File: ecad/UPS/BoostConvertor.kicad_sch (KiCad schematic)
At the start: 24 parts

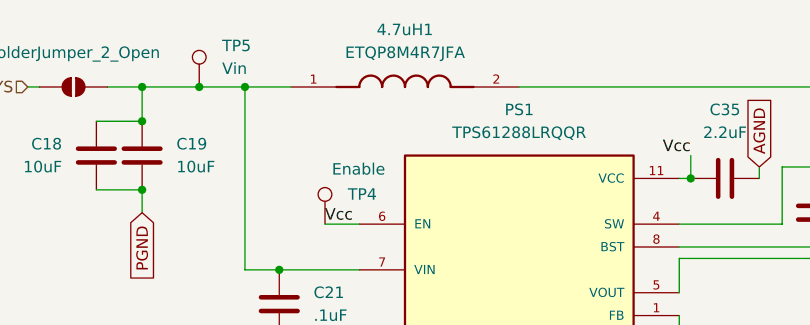
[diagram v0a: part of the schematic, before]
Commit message: Add switch
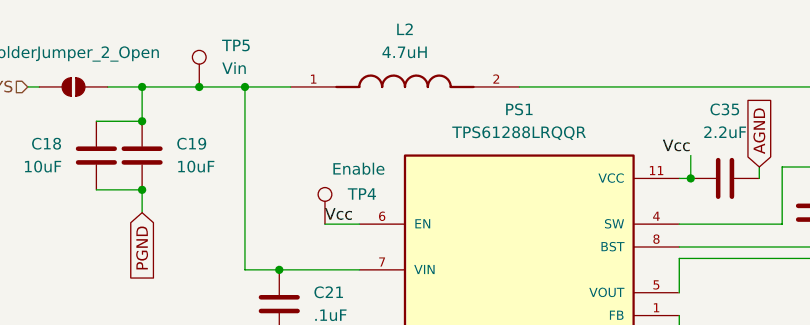
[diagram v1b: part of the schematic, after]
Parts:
- L2: renamed from 4.7uH1; value ETQP8M4R7JFA -> 4.7uH; footprint ETQP8M4R7JFA:IND_ETQP8M4R7JFA -> UPS:IND_ETQP8M4R7JFA
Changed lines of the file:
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@@
 		(dnp no)
 		(fields_autoplaced yes)
-		(property "Reference" "4.7uH1"
+		(property "Reference" "L2"
 			(at 92.71 45.72 0)
 			(effects
@@
 			)
 		)
-		(property "Value" "ETQP8M4R7JFA"
+		(property "Value" "4.7uH"
 			(at 92.71 48.26 0)
 			(effects
@@
 			)
 		)
-		(property "Footprint" "ETQP8M4R7JFA:IND_ETQP8M4R7JFA"
+		(property "Footprint" "UPS:IND_ETQP8M4R7JFA"
 			(at 92.71 52.07 0)
 			(effects
@@
 			(project ""
 				(path "/9d92b60a-4a6b-449c-b462-cab19e69d38c/66173f08-558e-4192-bd35-ba55c00529e3"
-					(reference "4.7uH1")
+					(reference "L2")
 					(unit 1)
 				)

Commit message: Output section of PCB
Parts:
- PS1: footprint TPS61288LRQQR:CONV_TPS61288LRQQR -> UPS:CONV_TPS61288LRQQR
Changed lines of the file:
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@@
 			)
 		)
-		(property "Footprint" "TPS61288LRQQR:CONV_TPS61288LRQQR"
+		(property "Footprint" "UPS:CONV_TPS61288LRQQR"
 			(at 105.41 77.47 0)
 			(effects

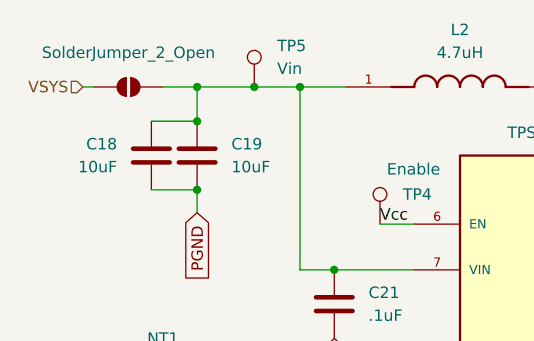
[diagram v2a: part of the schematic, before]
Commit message: replaced solder jumper with resistor
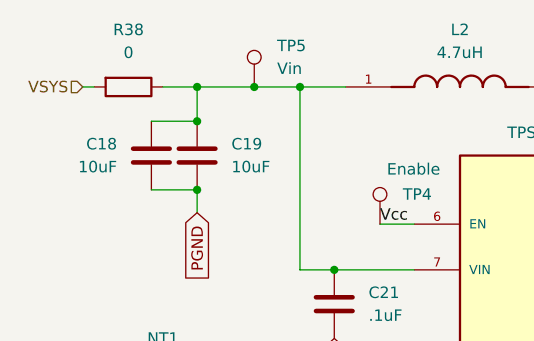
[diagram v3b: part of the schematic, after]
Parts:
- removed JP1: SolderJumper_2_Open, Jumper:SolderJumper-2_P1.3mm_Open_Pad1.0x1.5mm, symbol Jumper:SolderJumper_2_Open
- added R38: 0, Resistor_SMD:R_0805_2012Metric, symbol Device:R
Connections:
- net VSYS: now also R38.2
- net at C18.1, C19.1, C21.1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: now also R38.1
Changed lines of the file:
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@@
+	)
+	(symbol
+		(lib_id "Device:R")
+		(at 55.88 52.07 270)
+		(unit 1)
+		(exclude_from_sim no)
+		(in_bom yes)
+		(on_board yes)
+		(dnp no)
+		(fields_autoplaced yes)
+		(property "Reference" "R38"
+			(at 55.88 45.72 90)
+			(effects
+				(font
+					(size 1.27 1.27)
+				)
+			)
+		)
+		(property "Value" "0"
+			(at 55.88 48.26 90)
+			(effects
+				(font
+					(size 1.27 1.27)
+				)
+			)
+		)
+		(property "Footprint" "Resistor_SMD:R_0805_2012Metric"
+			(at 55.88 50.292 90)
+			(effects
+				(font
+					(size 1.27 1.27)
+				)
+				(hide yes)
+			)
+		)
+		(property "Datasheet" "~"
+			(at 55.88 52.07 0)
+			(effects
+				(font
+					(size 1.27 1.27)
+				)
+				(hide yes)
+			)
+		)
+		(property "Description" "Resistor"
+			(at 55.88 52.07 0)
+			(effects
+				(font
+					(size 1.27 1.27)
+				)
+				(hide yes)
+			)
+		)
+		(pin "2"
+		)
+		(pin "1"
+		)
+		(instances
+			(project ""
+				(path "/9d92b60a-4a6b-449c-b462-cab19e69d38c/66173f08-558e-4192-bd35-ba55c00529e3"
+					(reference "R38")
+					(unit 1)
+				)
+			)
+		)
 	)
 	(symbol
@@
 					(unit 1)
 				)
-			)
-		)
-	)
-	(symbol
-		(lib_id "Jumper:SolderJumper_2_Open")
-		(at 55.88 52.07 0)
-		(unit 1)
-		(exclude_from_sim no)
-		(in_bom no)
-		(on_board yes)
-		(dnp no)
-		(fields_autoplaced yes)
-		(property "Reference" "JP1"
-			(at 55.88 45.72 0)
-			(effects
-				(font
-					(size 1.27 1.27)
-				)
-				(hide yes)
-			)
-		)
-		(property "Value" "SolderJumper_2_Open"
-			(at 55.88 48.26 0)
-			(effects
-				(font
-					(size 1.27 1.27)
-				)
-			)
-		)
-		(property "Footprint" "Jumper:SolderJumper-2_P1.3mm_Open_Pad1.0x1.5mm"
-			(at 55.88 52.07 0)
-			(effects
-				(font
-					(size 1.27 1.27)
-				)
-				(hide yes)
-			)
-		)
-		(property "Datasheet" "~"
-			(at 55.88 52.07 0)
-			(effects
-				(font
-					(size 1.27 1.27)
-				)
-				(hide yes)
-			)
-		)
-		(property "Description" "Solder Jumper, 2-pole, open"
-			(at 55.88 52.07 0)
-			(effects
-				(font
-					(size 1.27 1.27)
-				)
-				(hide yes)
-			)
-		)
-		(pin "1"
-		)
-		(pin "2"
-		)
-		(instances
-			(project ""
-				(path "/9d92b60a-4a6b-449c-b462-cab19e69d38c/66173f08-558e-4192-bd35-ba55c00529e3"
-					(reference "JP1")
-					(unit 1)
-				)

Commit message: Updated Footprints
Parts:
- C20, C21, C22, C23, C3, C36: footprint Capacitor_SMD:C_0402_1005Metric_Pad0.74x0.62mm_HandSolder -> Capacitor_SMD:C_0603_1608Metric_Pad1.08x0.95mm_HandSolder
- R30, R31, R32: footprint Capacitor_SMD:C_0603_1608Metric_Pad1.08x0.95mm_HandSolder -> Resistor_SMD:R_0603_1608Metric_Pad0.98x0.95mm_HandSolder
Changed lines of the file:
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@@
 			)
 		)
-		(property "Footprint" "Capacitor_SMD:C_0402_1005Metric_Pad0.74x0.62mm_HandSolder"
+		(property "Footprint" "Capacitor_SMD:C_0603_1608Metric_Pad1.08x0.95mm_HandSolder"
 			(at 139.3952 69.85 0)
 			(effects
@@
 			)
 		)
-		(property "Footprint" "Capacitor_SMD:C_0402_1005Metric_Pad0.74x0.62mm_HandSolder"
+		(property "Footprint" "Capacitor_SMD:C_0603_1608Metric_Pad1.08x0.95mm_HandSolder"
 			(at 168.6052 87.63 0)
 			(effects
@@
 			)
 		)
-		(property "Footprint" "Capacitor_SMD:C_0603_1608Metric_Pad1.08x0.95mm_HandSolder"
+		(property "Footprint" "Resistor_SMD:R_0603_1608Metric_Pad0.98x0.95mm_HandSolder"
 			(at 135.382 93.98 90)
 			(effects
@@
 			)
 		)
-		(property "Footprint" "Capacitor_SMD:C_0402_1005Metric_Pad0.74x0.62mm_HandSolder"
+		(property "Footprint" "Capacitor_SMD:C_0603_1608Metric_Pad1.08x0.95mm_HandSolder"
 			(at 147.0152 90.17 0)
 			(effects
@@
 			)
 		)
-		(property "Footprint" "Capacitor_SMD:C_0402_1005Metric_Pad0.74x0.62mm_HandSolder"
+		(property "Footprint" "Capacitor_SMD:C_0603_1608Metric_Pad1.08x0.95mm_HandSolder"
 			(at 79.7052 80.01 0)
 			(effects
@@
 			)
 		)
-		(property "Footprint" "Capacitor_SMD:C_0603_1608Metric_Pad1.08x0.95mm_HandSolder"
+		(property "Footprint" "Resistor_SMD:R_0603_1608Metric_Pad0.98x0.95mm_HandSolder"
 			(at 155.702 74.93 90)
 			(effects
@@
 			)
 		)
-		(property "Footprint" "Capacitor_SMD:C_0402_1005Metric_Pad0.74x0.62mm_HandSolder"
+		(property "Footprint" "Capacitor_SMD:C_0603_1608Metric_Pad1.08x0.95mm_HandSolder"
 			(at 136.1948 82.55 0)
 			(effects
@@
 			)
 		)
-		(property "Footprint" "Capacitor_SMD:C_0603_1608Metric_Pad1.08x0.95mm_HandSolder"
+		(property "Footprint" "Resistor_SMD:R_0603_1608Metric_Pad0.98x0.95mm_HandSolder"
 			(at 155.702 85.09 90)
 			(effects
@@
 			)
 		)
-		(property "Footprint" "Capacitor_SMD:C_0402_1005Metric_Pad0.74x0.62mm_HandSolder"
+		(property "Footprint" "Capacitor_SMD:C_0603_1608Metric_Pad1.08x0.95mm_HandSolder"
 			(at 172.4152 78.74 0)
 			(effects

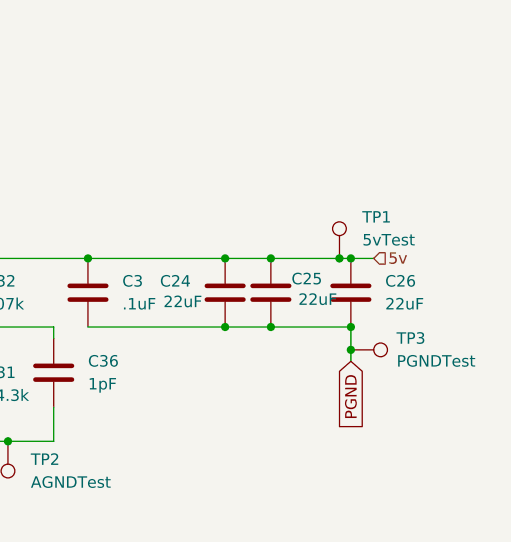
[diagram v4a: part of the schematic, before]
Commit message: Ty's VBATSENSE Changes
Let me know if I messed this part up, did a small amount
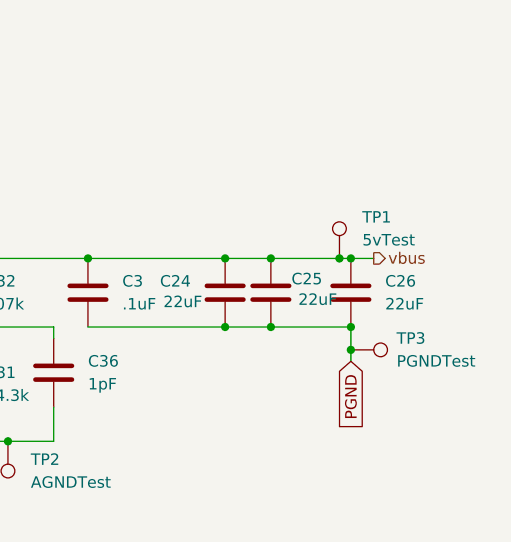
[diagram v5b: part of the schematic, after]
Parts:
- NT1: footprint (none) -> NetTie:NetTie-4_THT_Pad1.0mm
- R38: footprint Resistor_SMD:R_0805_2012Metric -> Resistor_SMD:R_1218_3246Metric_Pad1.22x4.75mm_HandSolder
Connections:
- net 5v renamed vbus
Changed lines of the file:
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@@
 		)
 	)
-	(hierarchical_label "5v"
-		(shape input)
+	(hierarchical_label "vbus"
+		(shape output)
 		(at 203.2 71.12 0)
 		(effects
@@
 			)
 		)
-		(property "Footprint" "Resistor_SMD:R_0805_2012Metric"
+		(property "Footprint" "Resistor_SMD:R_1218_3246Metric_Pad1.22x4.75mm_HandSolder"
 			(at 55.88 50.292 90)
 			(effects
@@
 			)
 		)
-		(property "Footprint" ""
+		(property "Footprint" "NetTie:NetTie-4_THT_Pad1.0mm"
 			(at 59.69 85.09 0)
 			(effects
